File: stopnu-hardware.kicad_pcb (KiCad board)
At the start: 4 copper layers, 94 x 131 mm, 64 parts, among them CN1 SM04B-SRSS-TB (LF)(SN), CN2 OQ0232510000G, CN3 OQ0232510000G, CN4 OQ0232510000G, CN5 OQ0232510000G, CN6 OQ0432510000G, J1 Conn_02x15_Odd_Even, U1 WIFI_KIT_32__V3_, U19 SY6280AAC, U2 74HCT1G125GW-Q100H, U3 LD1117V33, U4 74HCT1G125GW-Q100H, U5 LTV-817S, U6 LTV-817S, U7 LTV-817S

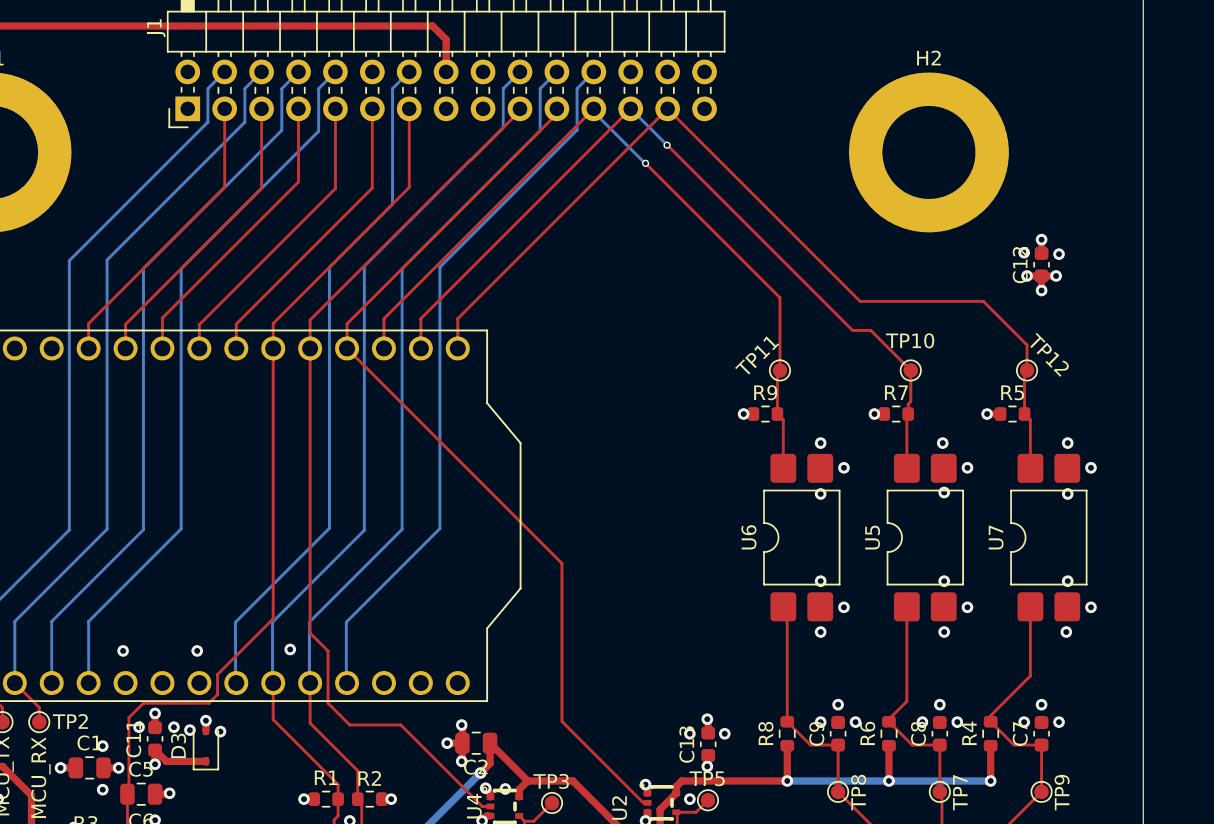
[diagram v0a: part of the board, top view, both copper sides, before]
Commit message: Rotate Optos 90' to handle pcb bending better.
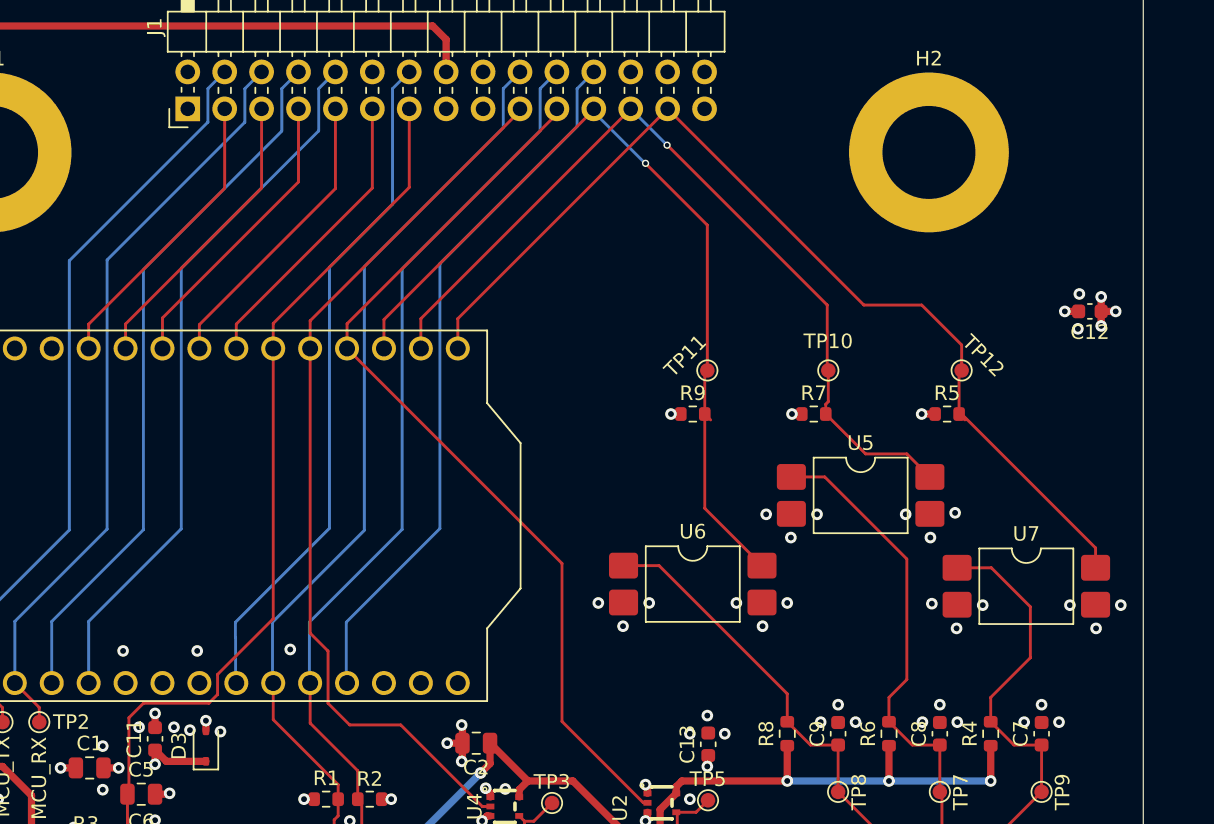
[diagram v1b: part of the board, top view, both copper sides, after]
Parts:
- moved U6 8.15 mm to (16.0, 46.7), turned to 0 degrees
- moved R7 5.68 mm to (24.3, 35.0)
- moved TP10 5.68 mm to (25.3, 32.0)
- moved U5 5.31 mm to (27.6, 40.6), turned to 0 degrees
- moved R9 5.00 mm to (16.0, 35.0)
- moved TP11 5.00 mm to (17.0, 32.0)
- moved C12 4.62 mm to (43.3, 27.9), turned to 180 degrees
- moved R5 4.50 mm to (33.5, 35.0)
- moved TP12 4.50 mm to (34.5, 32.0)
- moved U7 3.69 mm to (39.0, 46.9), turned to 0 degrees
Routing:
- net /Button IO/BUT_IN_02: track 24.6 -> 38.2 mm
- net /Button IO/BUT_IN_03: track 25.5 -> 34.8 mm
- net /GPIO07: track 62.4 -> 69.2 mm
- net /GPIO05: track 52.3 -> 59.0 mm
- net /Button IO/BUT_IN_01: track 26.8 -> 33.0 mm
- net /GPIO06: track 55.9 -> 58.1 mm
- net GND: track 29.4 -> 28.5 mm

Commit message: minor improvements.
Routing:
- net +3V3: track 19.0 -> 23.4 mm, vias 16 -> 19
- net /Button IO/BUT_IN_01: track 33.0 -> 31.5 mm
- net /Button IO/BUT_IN_02: track 38.2 -> 37.2 mm
- net GND: vias 86 -> 103

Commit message: Names of people that contributed.
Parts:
- added N2: Open Hardware, Symbol:OSHW-Logo2_9.8x8mm_SilkScreen, F.Cu at (11.0, 24.2)
- added N3: Ranzlogo, footprints:goatse_01, F.Cu at (-20.9, 42.0)
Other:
- board text added: "2025 Badge.Team Orange_Murker, Jhaand, NightOwl Ranzbak, R3nz3, Stoneshop CERN Open hardware License"

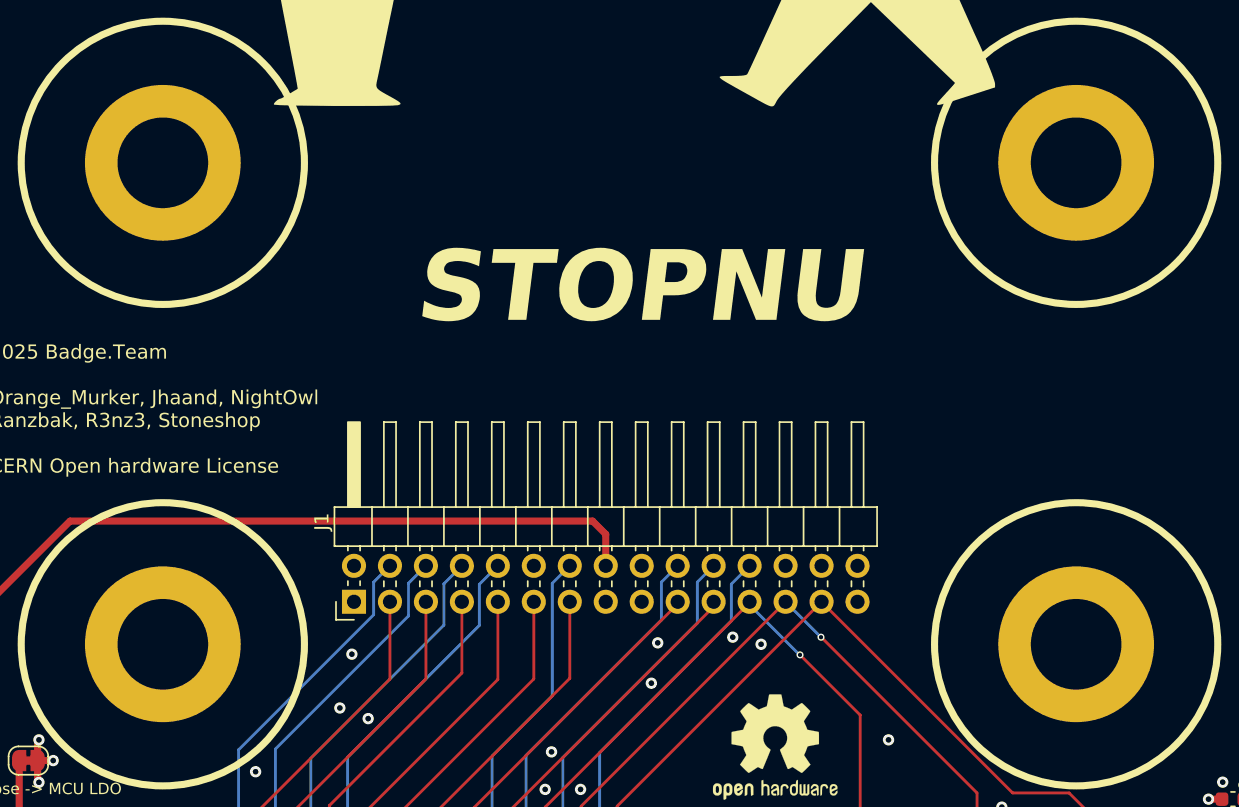
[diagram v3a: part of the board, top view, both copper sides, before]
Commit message: Mounting holes to 4.5mm.
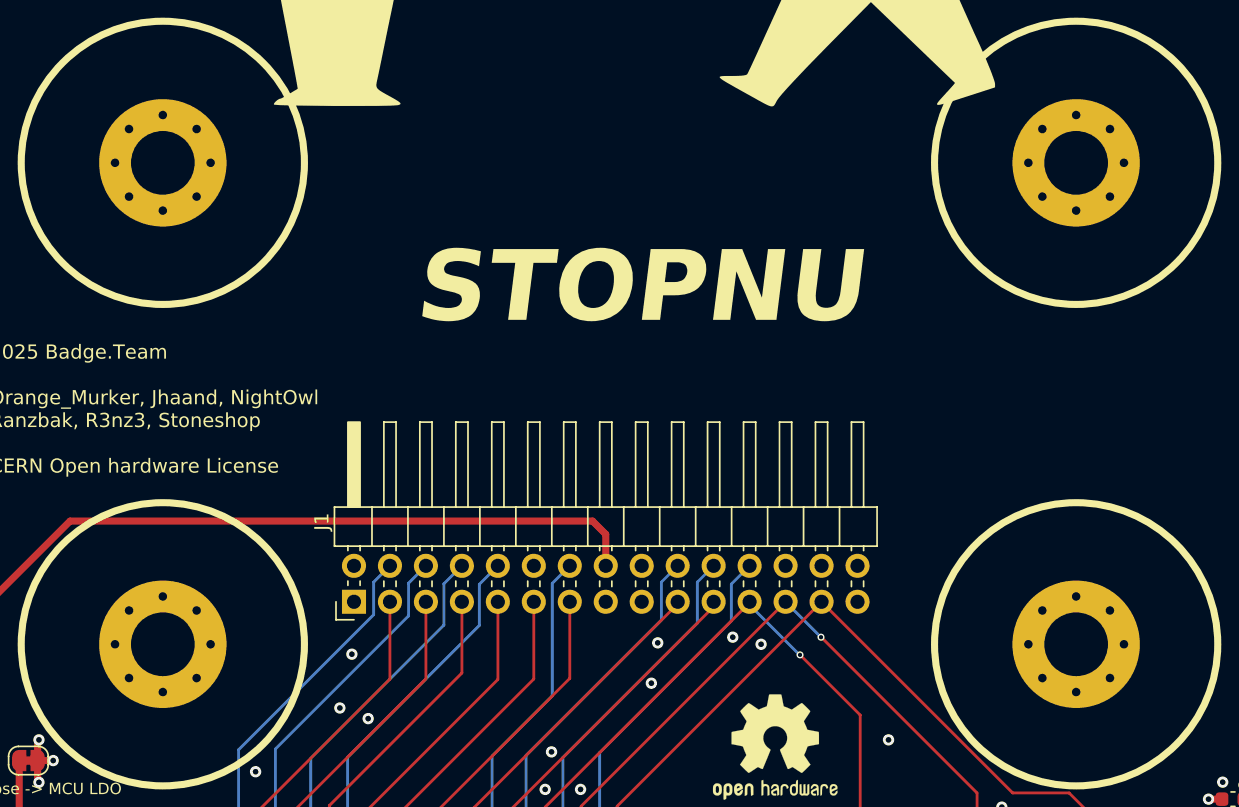
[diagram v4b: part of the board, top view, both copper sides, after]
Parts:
- H1, H2, H3, H4: footprint MountingHole:MountingHole_6.4mm_M6_DIN965_Pad -> MountingHole:MountingHole_4.5mm_Pad_Via

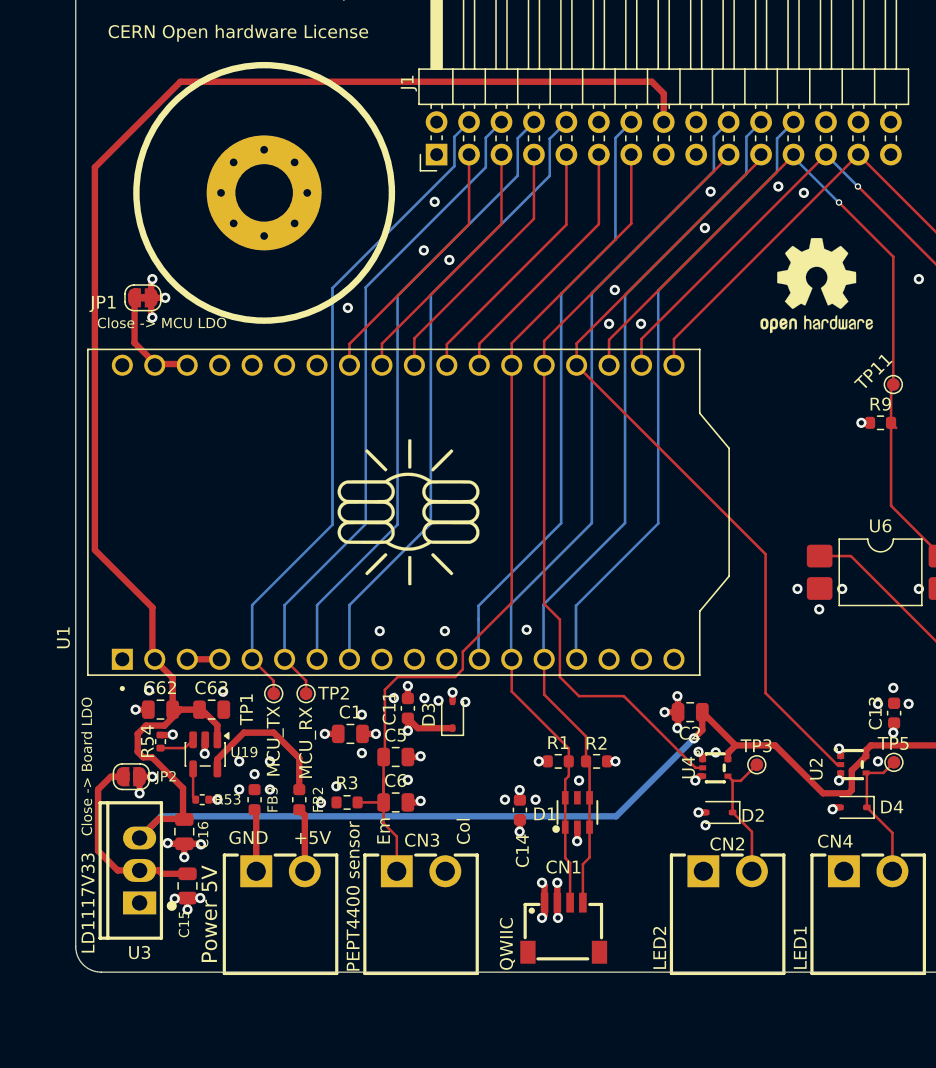
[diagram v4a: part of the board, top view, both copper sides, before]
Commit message: Fixed USB-pin routing, some other cleanups.
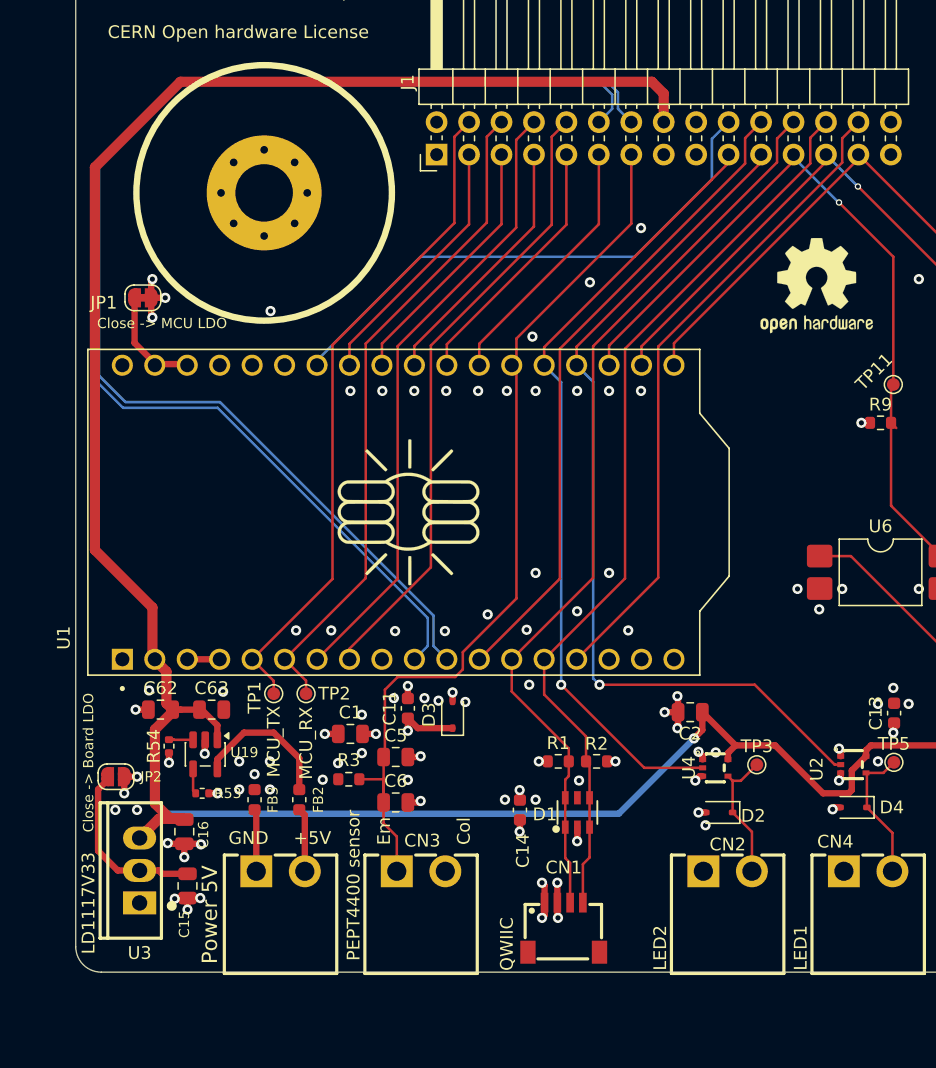
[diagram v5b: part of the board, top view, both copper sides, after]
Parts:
- moved R3 1.82 mm to (-25.6, 62.9)
- moved JP2 1.20 mm to (-43.9, 62.7)
- moved R54 0.75 mm to (-39.7, 60.3), turned to -90 degrees
- moved R53 0.50 mm to (-37.1, 64.0)
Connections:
- J1 pad 12: /GPIO34 -> /USB_D-
- J1 pad 14: /GPIO33 -> /USB_D+
- J1 pad 20: /GPIO47 -> /GPIO42
- J1 pad 22: /GPIO48 -> /GPIO33
- J1 pad 24: /GPIO26 -> /GPIO47
- J1 pad 26: unconnected-(J1-Pin_26-Pad26) -> /GPIO48
- J1 pad 28: unconnected-(J1-Pin_28-Pad28) -> /GPIO26
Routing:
- net /USB_D+: track 0.00 -> 101.4 mm
- net /USB_D-: track 0.00 -> 99.9 mm
- net /GPIO42: track 0.00 -> 42.2 mm
- net /GPIO04: track 62.4 -> 69.3 mm, vias 0 -> 1
- net /GPIO33: track 47.0 -> 51.2 mm
- net /GPIO48: track 69.5 -> 71.5 mm
- net /GPIO26: track 49.1 -> 51.2 mm
- net /GPIO47: track 70.3 -> 72.4 mm
- net +5V: track 213.7 -> 211.7 mm
- net Net-(JP2-A): track 14.9 -> 14.0 mm
- net Net-(U19-SET): track 2.82 -> 2.29 mm
- net /GPIO03: track 61.4 -> 61.7 mm, vias 0 -> 1
- net GND: track 28.5 -> 28.3 mm, vias 103 -> 116
